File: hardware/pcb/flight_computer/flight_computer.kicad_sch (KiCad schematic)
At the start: 12 parts, among them J2 BATT_TERMINAL, J3 5V Terminal, J4 Pyro 1, J5 Pyro 2, J8 Conn_01x02, J9 Aux Ports

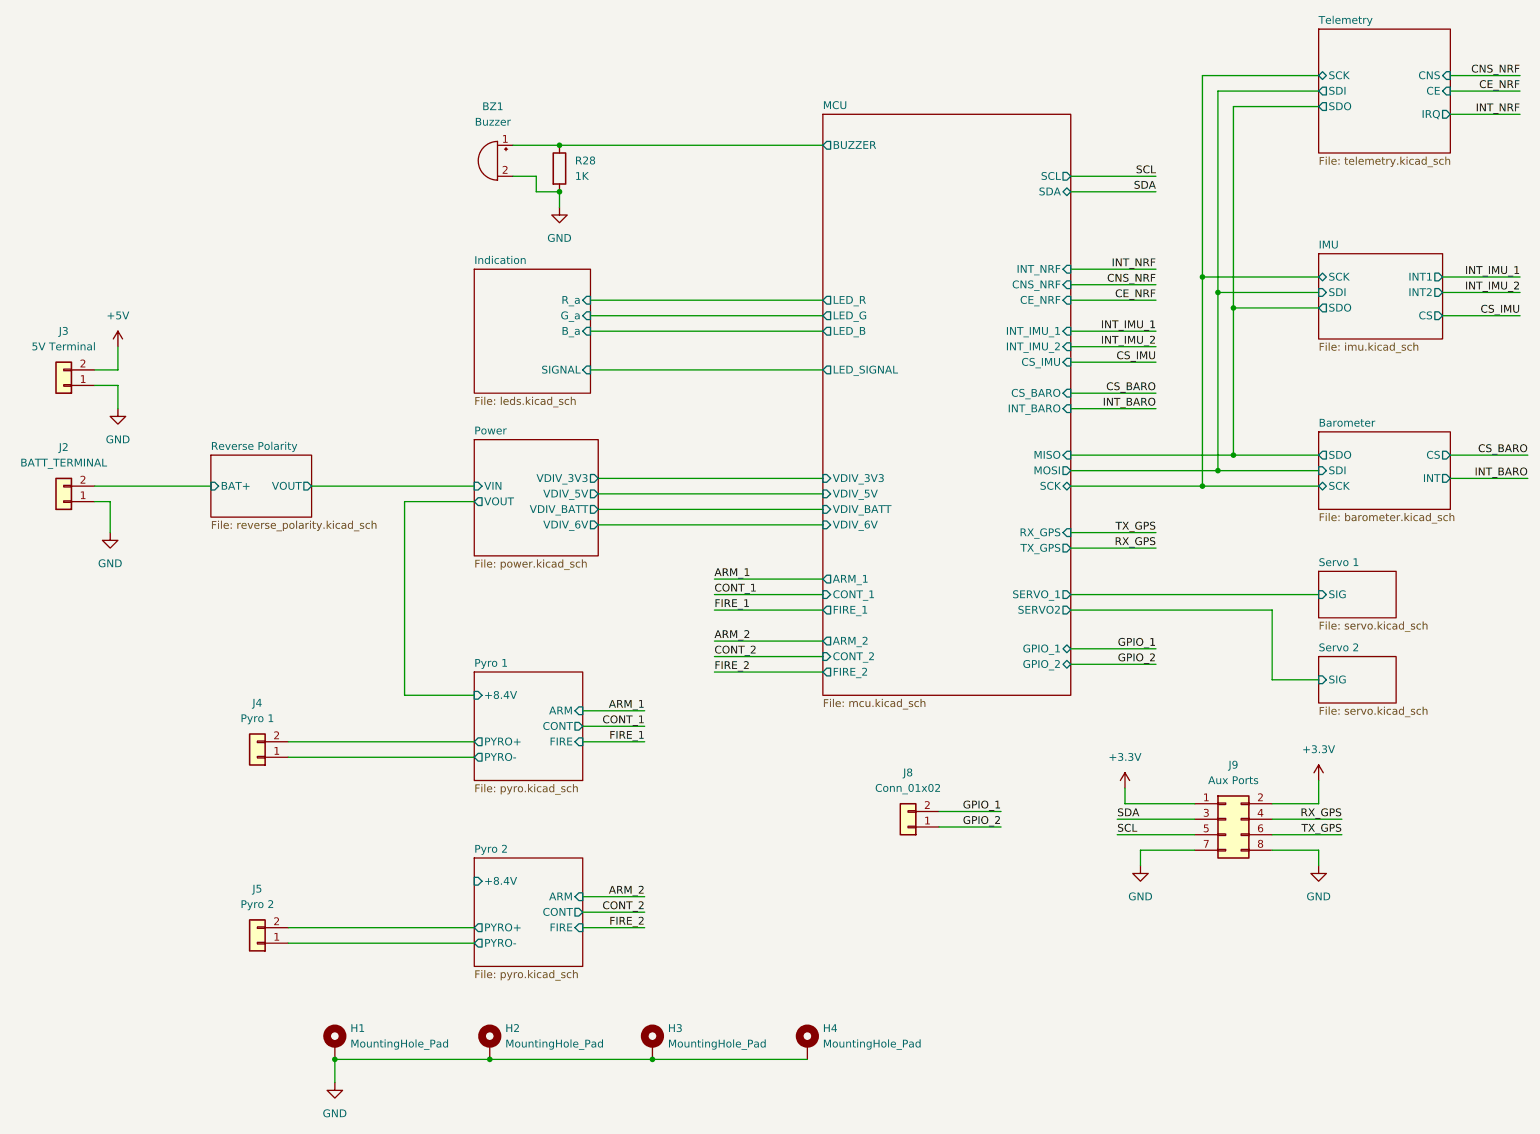
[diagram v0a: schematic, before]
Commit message: Added 3D model
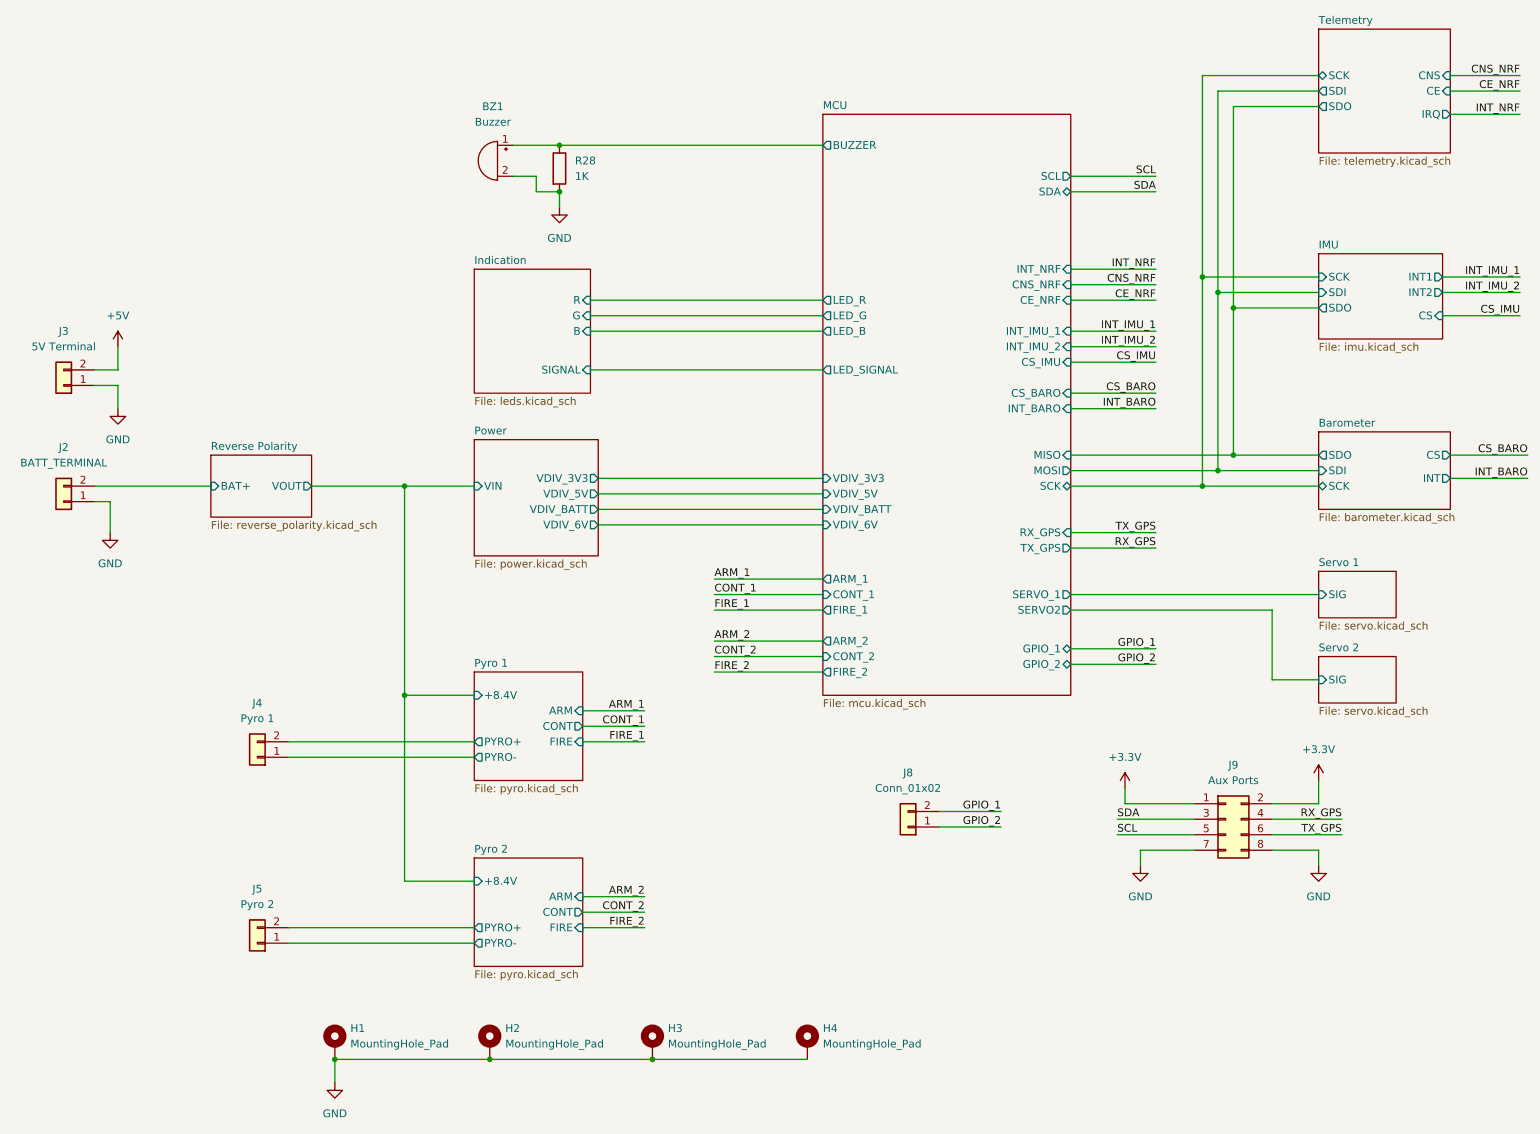
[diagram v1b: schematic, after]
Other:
- sheet Indication ports: added B, G, R; removed B_a, G_a, R_a
- sheet Power ports: added none; removed VOUT
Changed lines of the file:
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@@
 	)
 	(junction
+		(at 83.82 128.27)
+		(diameter 0)
+		(color 0 0 0 0)
+	)
+	(junction
 		(at 217.17 62.23)
 		(diameter 0)
@@
 	)
 	(junction
+		(at 83.82 93.98)
+		(diameter 0)
+		(color 0 0 0 0)
+	)
+	(junction
 		(at 109.22 45.72)
 		(diameter 0)
@@
 	(wire
 		(pts
-			(xy 83.82 96.52) (xy 83.82 128.27)
+			(xy 83.82 93.98) (xy 83.82 128.27)
 		)
 		(stroke
@@
 	(wire
 		(pts
+			(xy 83.82 93.98) (xy 95.25 93.98)
+		)
+		(stroke
+			(width 0)
+			(type default)
+		)
+	)
+	(wire
+		(pts
 			(xy 114.3 68.58) (xy 152.4 68.58)
 		)
@@
 	(wire
 		(pts
-			(xy 68.58 93.98) (xy 95.25 93.98)
+			(xy 68.58 93.98) (xy 83.82 93.98)
 		)
 		(stroke
@@
 	(wire
 		(pts
+			(xy 83.82 128.27) (xy 83.82 158.75)
+		)
+		(stroke
+			(width 0)
+			(type default)
+		)
+	)
+	(wire
+		(pts
 			(xy 109.22 38.1) (xy 152.4 38.1)
 		)
@@
 	(wire
 		(pts
-			(xy 193.04 120.65) (xy 207.01 120.65)
+			(xy 95.25 158.75) (xy 83.82 158.75)
 		)
 		(stroke
@@
 	(wire
 		(pts
-			(xy 200.66 148.59) (xy 213.36 148.59)
+			(xy 193.04 120.65) (xy 207.01 120.65)
 		)
 		(stroke
@@
 	(wire
 		(pts
-			(xy 113.03 163.83) (xy 123.19 163.83)
+			(xy 200.66 148.59) (xy 213.36 148.59)
 		)
 		(stroke
@@
 	(wire
 		(pts
-			(xy 36.83 77.47) (xy 33.02 77.47)
+			(xy 113.03 163.83) (xy 123.19 163.83)
 		)
 		(stroke
@@
 	(wire
 		(pts
-			(xy 114.3 74.93) (xy 152.4 74.93)
+			(xy 36.83 77.47) (xy 33.02 77.47)
 		)
 		(stroke
@@
 	(wire
 		(pts
-			(xy 95.25 96.52) (xy 83.82 96.52)
+			(xy 114.3 74.93) (xy 152.4 74.93)
 		)
 		(stroke
@@
 			)
 		)
-		(pin "B_a" input
-			(at 114.3 68.58 0)
+		(pin "SIGNAL" input
+			(at 114.3 74.93 0)
 			(effects
 				(font
@@
 			)
 		)
-		(pin "G_a" input
-			(at 114.3 66.04 0)
+		(pin "B" input
+			(at 114.3 68.58 0)
 			(effects
 				(font
@@
 			)
 		)
-		(pin "R_a" input
-			(at 114.3 63.5 0)
+		(pin "G" input
+			(at 114.3 66.04 0)
 			(effects
 				(font
@@
 			)
 		)
-		(pin "SIGNAL" input
-			(at 114.3 74.93 0)
+		(pin "R" input
+			(at 114.3 63.5 0)
 			(effects
 				(font
@@
 			)
 		)
-		(pin "VOUT" output
-			(at 95.25 96.52 180)
-			(effects
-				(font
-					(size 1.27 1.27)
-				)
-				(justify left)
-			)
-		)
 		(pin "VDIV_3V3" output
 			(at 115.57 92.71 0)
@@
 			)
 		)
-		(pin "CS" output
+		(pin "CS" input
 			(at 254 66.04 0)
 			(effects
@@
 			)
 		)
-		(pin "SCK" bidirectional
+		(pin "SCK" input
 			(at 233.68 59.69 180)
 			(effects
